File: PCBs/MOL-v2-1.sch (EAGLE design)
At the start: 24 parts, among them IC1 ULN2803, IC2 ULN2803, J1 SERVO1, J2 SERVO2, J3 STRIPS, J4 ACTUATORS

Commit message: MOL updates
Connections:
- removed net A11: U$3.50/A24
- removed net A12: U$3.49/A23
- net +3V3: now also JOY1.1, JOY2.1; no longer JOY1.2, JOY2.2
- net AGND: now also JOY1.2, JOY2.2; no longer JOY1.1, JOY2.1
- net AN11: now also U$3.50/A24
- net AN12: now also U$3.49/A23
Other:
- moved on the sheet: AN-IN-1, AN-IN-2, AN-IN-3, AN-IN-4, IC1, IC2, J1, J2, J3, J4, JOY1, JOY2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

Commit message: reroute + Arduino stuff
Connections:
- net LED1: now also U$3.55
- net LED3: no longer U$3.55
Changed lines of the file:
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@@
-</segment>
-<segment>
-<wire x1="96.52" y1="254" x2="109.22" y2="254" width="0.1524" layer="91"/>
-<pinref part="U$3" gate="G$1" pin="55"/>
-<label x="109.22" y="254" size="1.016" layer="95" xref="yes"/>
 </segment>
 <segment>
@@
 <pinref part="J3" gate="G$1" pin="7"/>
 </segment>
-</net>
+<segment>
+<wire x1="96.52" y1="254" x2="109.22" y2="254" width="0.1524" layer="91"/>
+<pinref part="U$3" gate="G$1" pin="55"/>
+<label x="109.22" y="254" size="1.016" layer="95" xref="yes"/>
+</segment>
+</net>

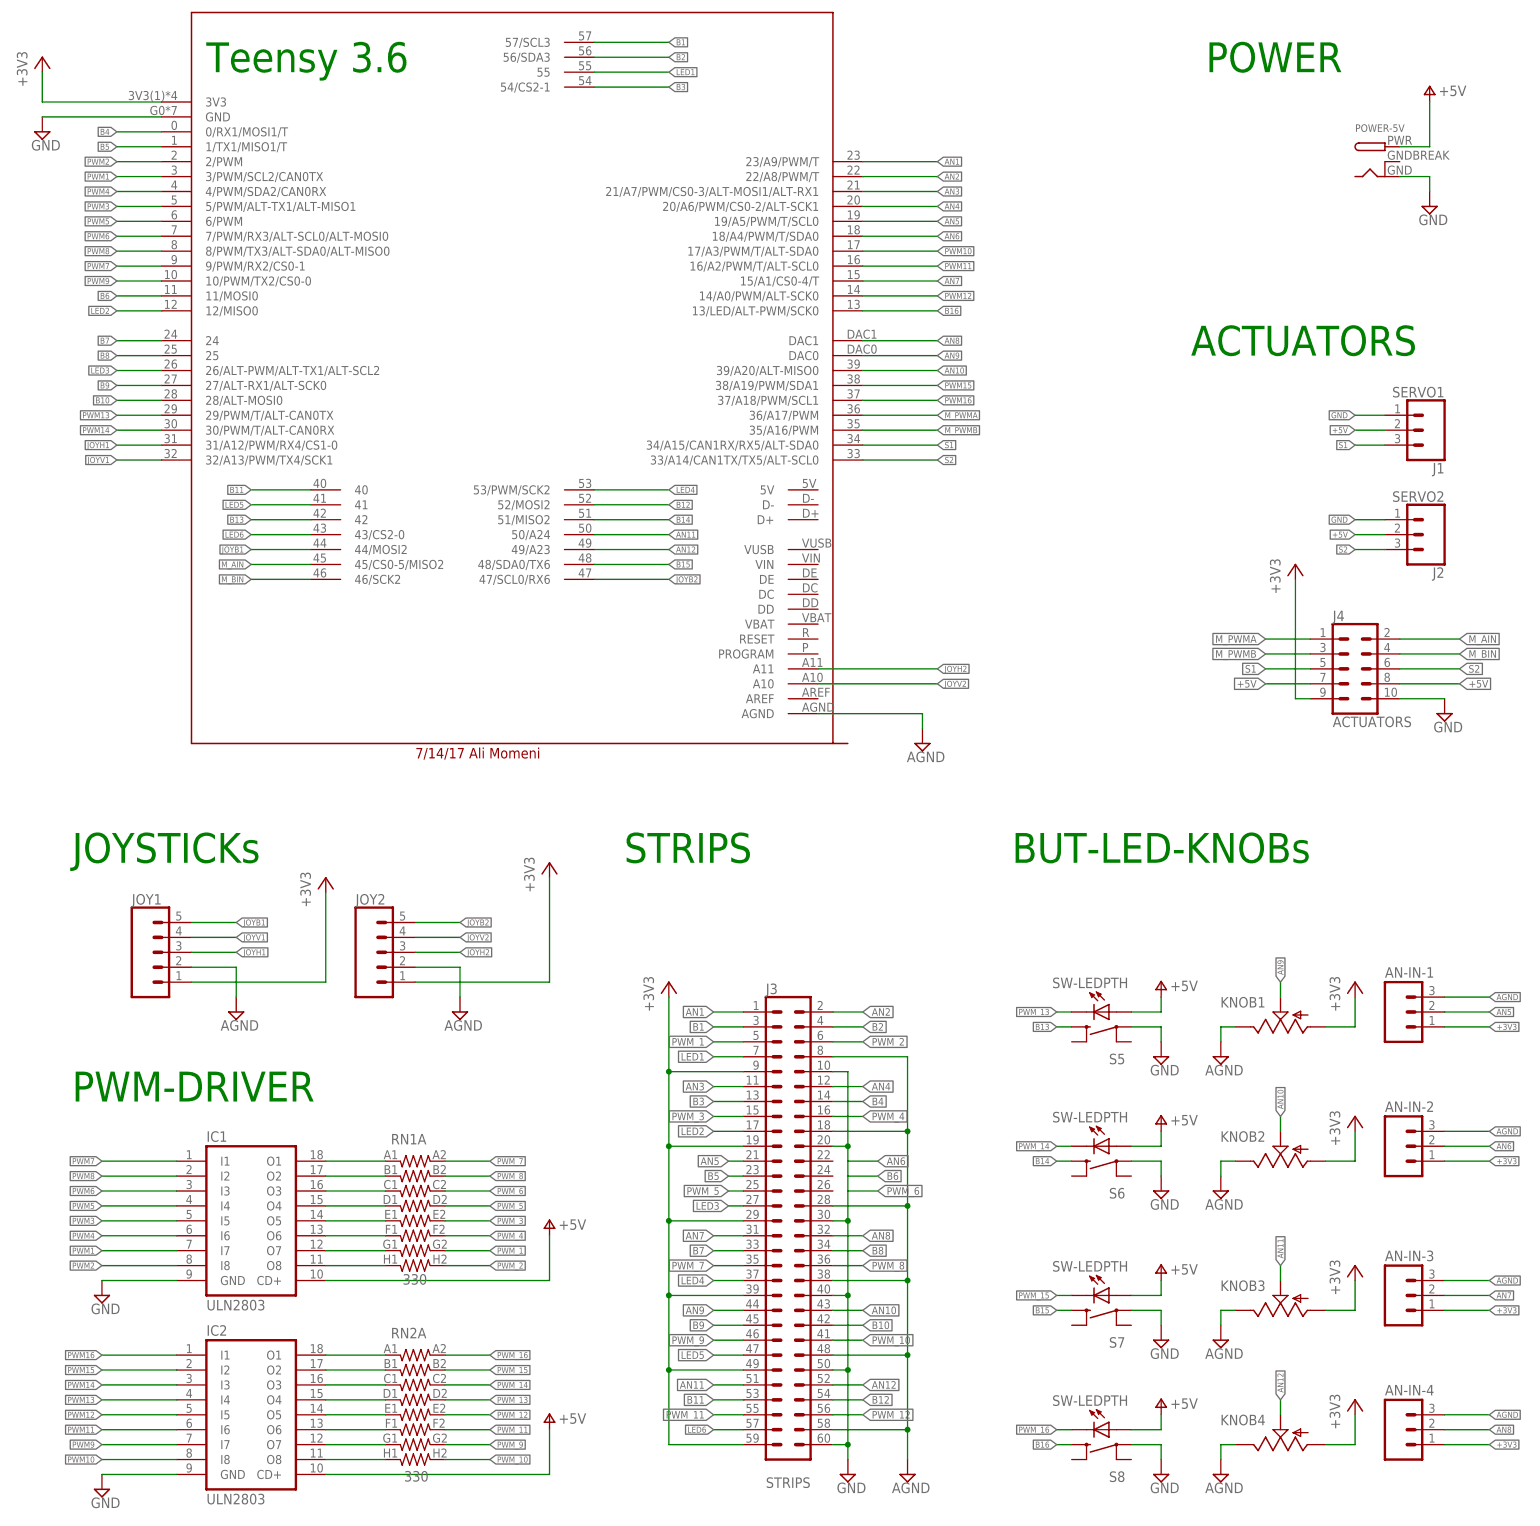
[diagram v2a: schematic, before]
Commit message: updates to teensy breakout
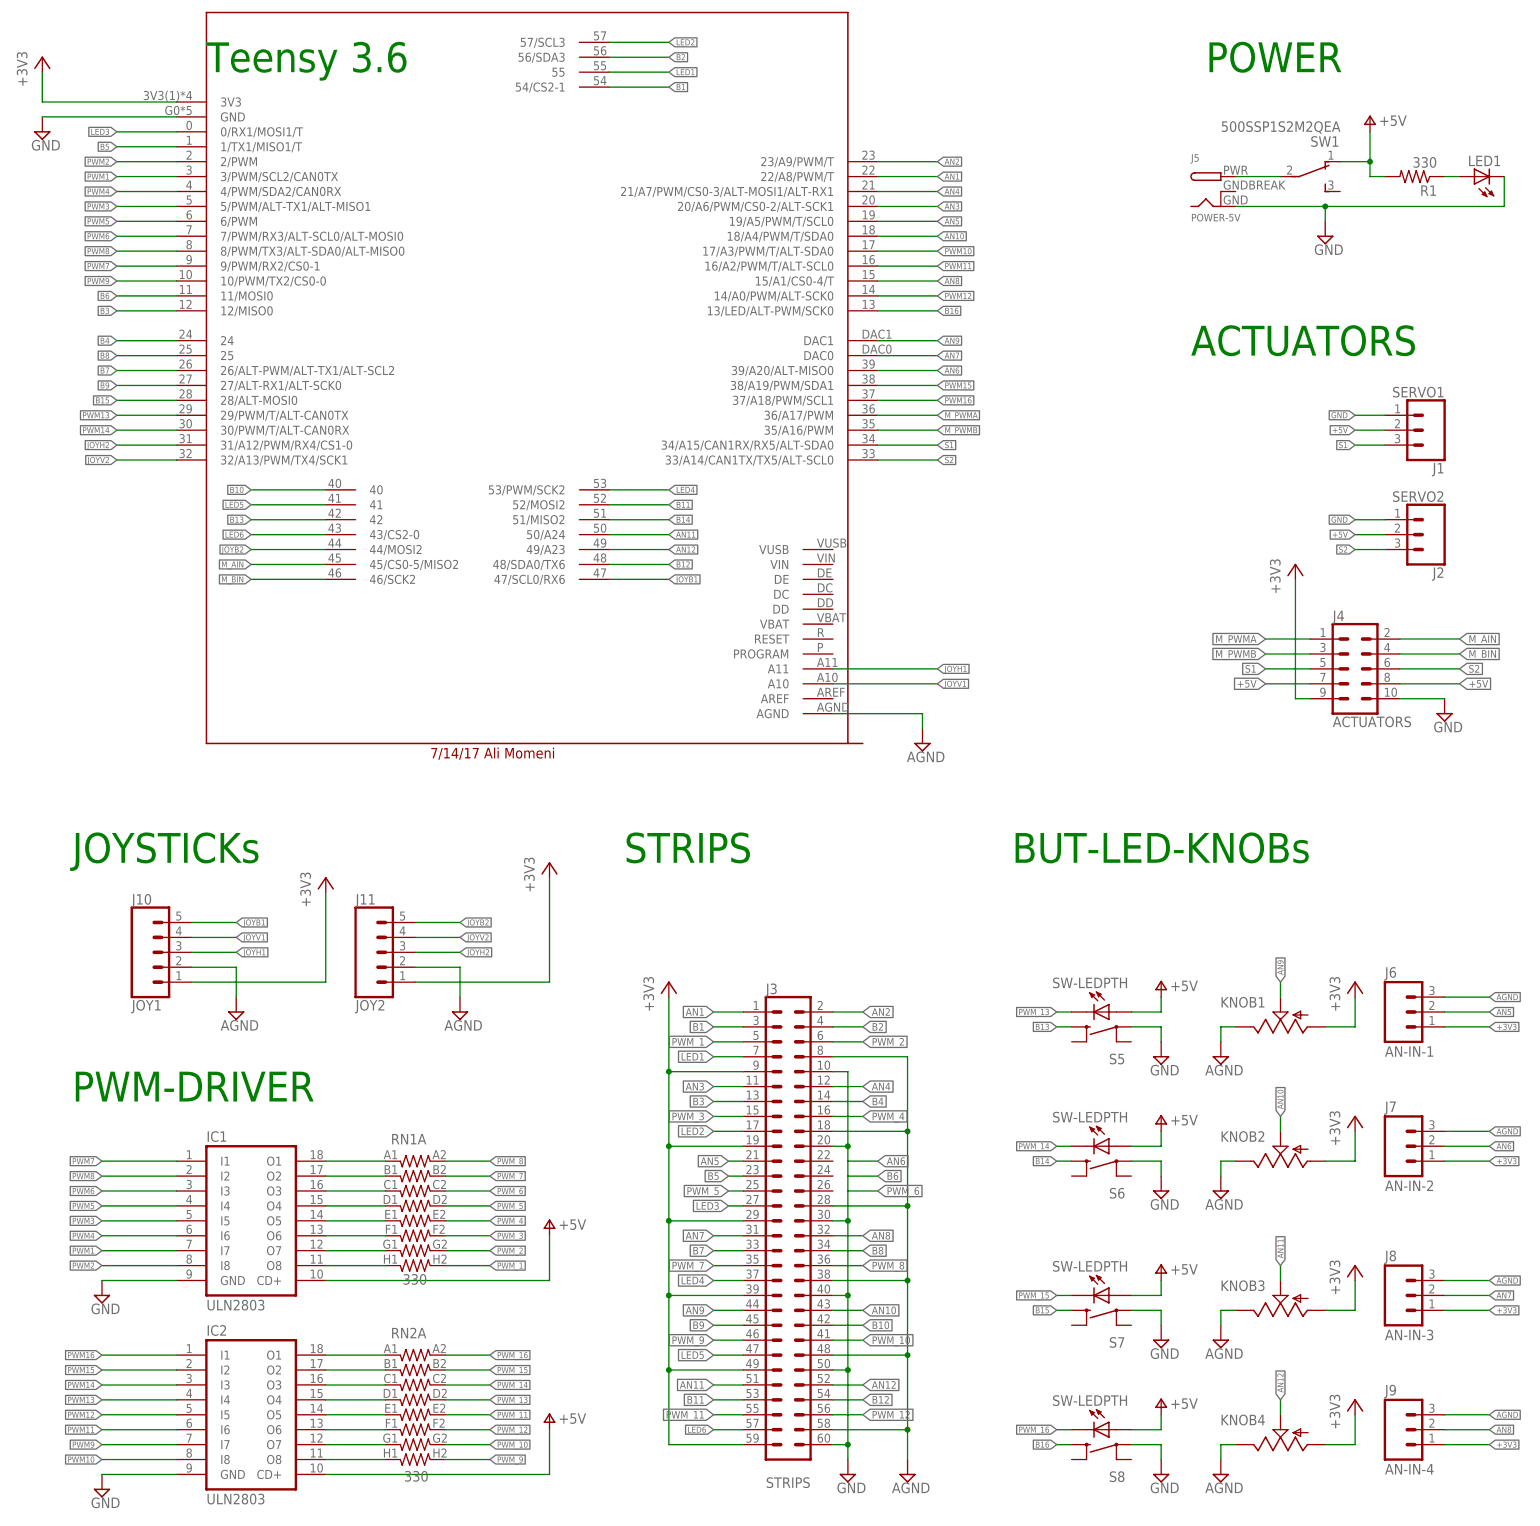
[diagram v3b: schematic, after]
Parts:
- removed POWER-5V: (no value), adafruit:DCBARRELPTH
- removed U$3: TEENSY3_6--ALLPINS_ALI, CMU-ArtFab:TEENSY3_6--ALLPINS_ALI
- added J5: POWER-5V, adafruit:DCBARRELPTH
- added LED1: (no value), led:LED3MM
- added R1: 330, resistor:R-US_0204/7
- added SW1: 500SSP1S2M2QEA, CMU-ArtFab:SWITCH_SPDT500SSP1S2M2QEA
- added U$1: TEENSY3_6-ALI_NO-USB-HOST, CMU-ArtFab:TEENSY3_6-ALI_NO-USB-HOST
- J10: value (none) -> JOY1
- J11: value (none) -> JOY2
- J6: value (none) -> AN-IN-1
- J7: value (none) -> AN-IN-2
- J8: value (none) -> AN-IN-3
- J9: value (none) -> AN-IN-4
- renumbered AN-IN-1 to J6, AN-IN-2 to J7, AN-IN-3 to J8, AN-IN-4 to J9, JOY1 to J10, JOY2 to J11
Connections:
- new net N$1: J5.PWR, SW1.2
- new net N$2: LED1.A, R1.1
- net +3V3: now also U$1.3V3; no longer U$3.3V3
- net +5V: now also R1.2, SW1.1; no longer POWER-5V.PWR
- net AGND: now also U$1.AGND; no longer U$3.AGND
- net AN1: now also U$1.22/A8/PWM/T; no longer U$3.23/A9/PWM/T
- net AN10: now also U$1.18/A4/PWM/T/SDA0; no longer U$3.39/A20/ALT-MISO0
- net AN11: now also U$1.50/A24; no longer U$3.50/A24
- net AN12: now also U$1.49/A23; no longer U$3.49/A23
- net AN2: now also U$1.23/A9/PWM/T; no longer U$3.22/A8/PWM/T
- net AN3: now also U$1.20/A6/PWM/CS0-2/ALT-SCK1; no longer U$3.21/A7/PWM/CS0-3/ALT-MOSI1/ALT-RX1
- net AN4: now also U$1.21/A7/PWM/CS0-3/ALT-MOSI1/ALT-RX1; no longer U$3.20/A6/PWM/CS0-2/ALT-SCK1
- net AN5: now also U$1.19/A5/PWM/T/SCL0; no longer U$3.19/A5/PWM/T/SCL0
- net AN6: now also U$1.39/A20/ALT-MISO0; no longer U$3.18/A4/PWM/T/SDA0
- net AN7: now also U$1.DAC0; no longer U$3.15/A1/CS0-4/T
- net AN8: now also U$1.15/A1/CS0-4/T; no longer U$3.DAC1
- net AN9: now also U$1.DAC1; no longer U$3.DAC0
- net B1: now also U$1.54/CS2-1; no longer U$3.57/SCL3
- net B10: now also U$1.40; no longer U$3.28/ALT-MOSI0
- net B11: now also U$1.52/MOSI2; no longer U$3.40
- net B12: now also U$1.48/SDA0/TX6; no longer U$3.52/MOSI2
- net B13: now also U$1.42; no longer U$3.42
- net B14: now also U$1.51/MISO2; no longer U$3.51/MISO2
- net B15: now also U$1.28/ALT-MOSI0; no longer U$3.48/SDA0/TX6
- net B16: now also U$1.13/LED/ALT-PWM/SCK0; no longer U$3.13/LED/ALT-PWM/SCK0
- net B2: now also U$1.56/SDA3; no longer U$3.56/SDA3
- net B3: now also U$1.12/MISO0; no longer U$3.54/CS2-1
- net B4: now also U$1.24; no longer U$3.0/RX1/MOSI1/T
- net B5: now also U$1.1/TX1/MISO1/T; no longer U$3.1/TX1/MISO1/T
- net B6: now also U$1.11/MOSI0; no longer U$3.11/MOSI0
- net B7: now also U$1.26/ALT-PWM/ALT-TX1/ALT-SCL2; no longer U$3.24
- net B8: now also U$1.25; no longer U$3.25
- net B9: now also U$1.27/ALT-RX1/ALT-SCK0; no longer U$3.27/ALT-RX1/ALT-SCK0
- net GND: now also J5.GND, LED1.C, U$1.GND; no longer POWER-5V.GND, U$3.GND
- net JOYB1: now also U$1.47/SCL0/RX6; no longer U$3.44/MOSI2
- net JOYB2: now also U$1.44/MOSI2; no longer U$3.47/SCL0/RX6
- net JOYH1: now also U$1.A11; no longer U$3.31/A12/PWM/RX4/CS1-0
- net JOYH2: now also U$1.31/A12/PWM/RX4/CS1-0; no longer U$3.A11
- net JOYV1: now also U$1.A10; no longer U$3.32/A13/PWM/TX4/SCK1
- net JOYV2: now also U$1.32/A13/PWM/TX4/SCK1; no longer U$3.A10
- net LED1: now also U$1.55; no longer U$3.55
- net LED2: now also U$1.57/SCL3; no longer U$3.12/MISO0
- net LED3: now also U$1.0/RX1/MOSI1/T; no longer U$3.26/ALT-PWM/ALT-TX1/ALT-SCL2
- net LED4: now also U$1.53/PWM/SCK2; no longer U$3.53/PWM/SCK2
- net LED5: now also U$1.41; no longer U$3.41
- net LED6: now also U$1.43/CS2-0; no longer U$3.43/CS2-0
- net M_AIN: now also U$1.45/CS0-5/MISO2; no longer U$3.45/CS0-5/MISO2
- net M_BIN: now also U$1.46/SCK2; no longer U$3.46/SCK2
- net M_PWMA: now also U$1.36/A17/PWM; no longer U$3.36/A17/PWM
- net M_PWMB: now also U$1.35/A16/PWM; no longer U$3.35/A16/PWM
- net PWM1: now also U$1.3/PWM/SCL2/CAN0TX; no longer U$3.3/PWM/SCL2/CAN0TX
- net PWM10: now also U$1.17/A3/PWM/T/ALT-SDA0; no longer U$3.17/A3/PWM/T/ALT-SDA0
- net PWM11: now also U$1.16/A2/PWM/T/ALT-SCL0; no longer U$3.16/A2/PWM/T/ALT-SCL0
- net PWM12: now also U$1.14/A0/PWM/ALT-SCK0; no longer U$3.14/A0/PWM/ALT-SCK0
- net PWM13: now also U$1.29/PWM/T/ALT-CAN0TX; no longer U$3.29/PWM/T/ALT-CAN0TX
- net PWM14: now also U$1.30/PWM/T/ALT-CAN0RX; no longer U$3.30/PWM/T/ALT-CAN0RX
- net PWM15: now also U$1.38/A19/PWM/SDA1; no longer U$3.38/A19/PWM/SDA1
- net PWM16: now also U$1.37/A18/PWM/SCL1; no longer U$3.37/A18/PWM/SCL1
- net PWM2: now also U$1.2/PWM; no longer U$3.2/PWM
- net PWM3: now also U$1.5/PWM/ALT-TX1/ALT-MISO1; no longer U$3.5/PWM/ALT-TX1/ALT-MISO1
- net PWM4: now also U$1.4/PWM/SDA2/CAN0RX; no longer U$3.4/PWM/SDA2/CAN0RX
- net PWM5: now also U$1.6/PWM; no longer U$3.6/PWM
- net PWM6: now also U$1.7/PWM/RX3/ALT-SCL0/ALT-MOSI0; no longer U$3.7/PWM/RX3/ALT-SCL0/ALT-MOSI0
- net PWM7: now also U$1.9/PWM/RX2/CS0-1; no longer U$3.9/PWM/RX2/CS0-1
- net PWM8: now also U$1.8/PWM/TX3/ALT-SDA0/ALT-MISO0; no longer U$3.8/PWM/TX3/ALT-SDA0/ALT-MISO0
- net PWM9: now also U$1.10/PWM/TX2/CS0-0; no longer U$3.10/PWM/TX2/CS0-0
- net PWM_1: now also RN1H.2; no longer RN1G.2
- net PWM_10: now also RN2G.2; no longer RN2H.2
- net PWM_11: now also RN2E.2; no longer RN2F.2
- net PWM_12: now also RN2F.2; no longer RN2E.2
- net PWM_2: now also RN1G.2; no longer RN1H.2
- net PWM_3: now also RN1F.2; no longer RN1E.2
- net PWM_4: now also RN1E.2; no longer RN1F.2
- net PWM_7: now also RN1B.2; no longer RN1A.2
- net PWM_8: now also RN1A.2; no longer RN1B.2
- net PWM_9: now also RN2H.2; no longer RN2G.2
- net S1: now also U$1.34/A15/CAN1RX/RX5/ALT-SDA0; no longer U$3.34/A15/CAN1RX/RX5/ALT-SDA0
- net S2: now also U$1.33/A14/CAN1TX/TX5/ALT-SCL0; no longer U$3.33/A14/CAN1TX/TX5/ALT-SCL0
